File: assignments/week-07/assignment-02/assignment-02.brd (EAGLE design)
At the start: 68.6 x 53.3 mm, 6 parts

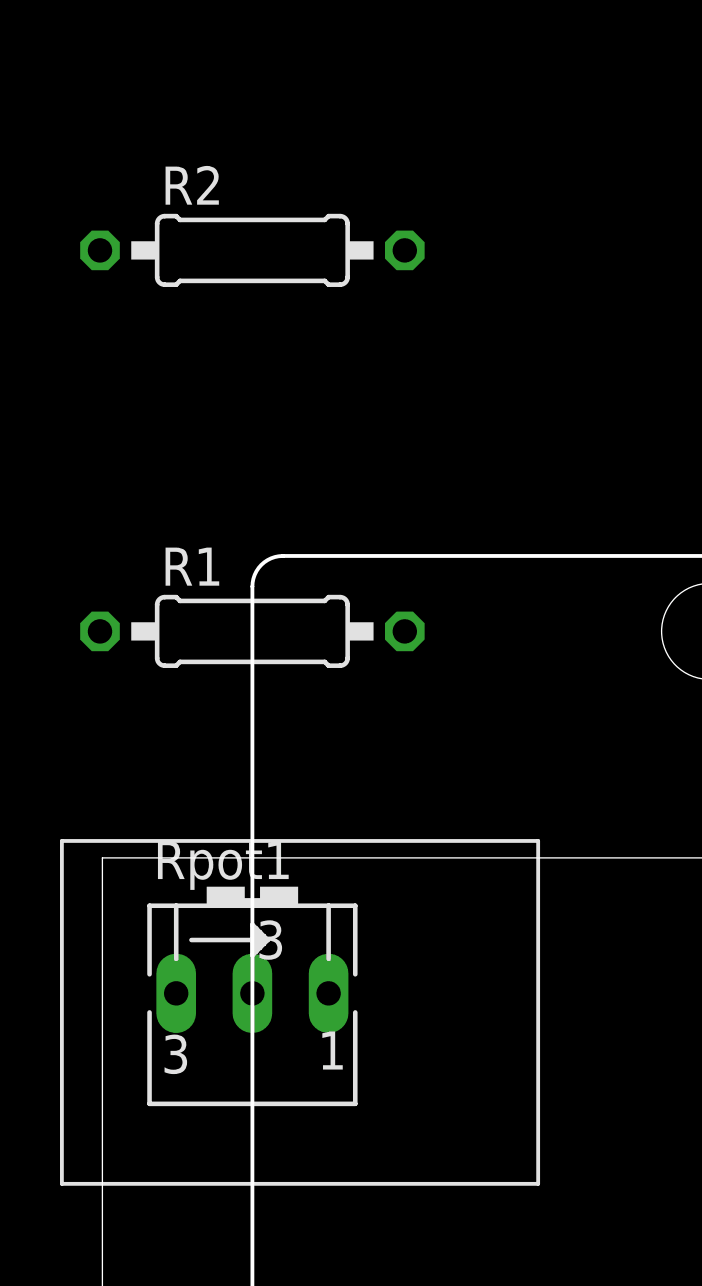
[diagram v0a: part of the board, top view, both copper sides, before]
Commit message: Remove Serial usage
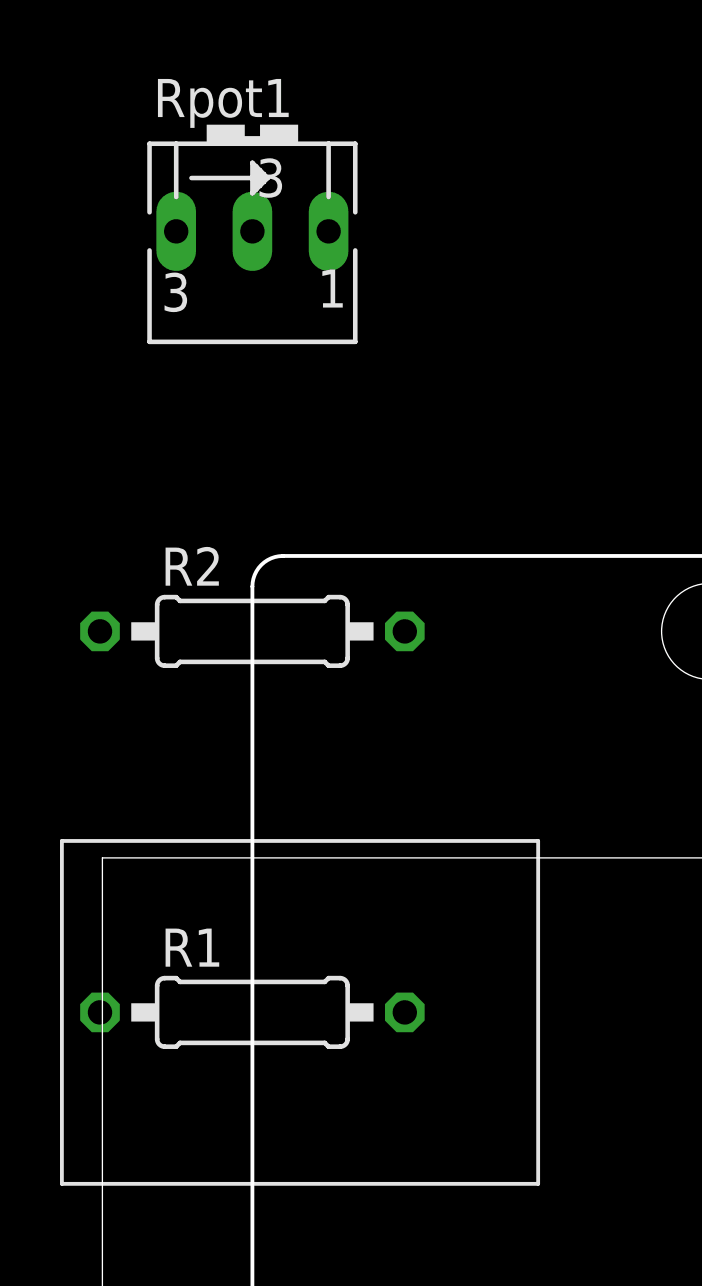
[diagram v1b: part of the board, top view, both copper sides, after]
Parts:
- moved Rpot1 25.4 mm to (5.00, 73.6)
- moved R2 12.7 mm to (5.00, 60.9)
- moved R1 12.7 mm to (5.00, 48.2)
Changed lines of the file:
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@@
 </autorouter>
 <elements>
-<element value="" name="U1" library="AUTODESK_CIRCUITS_BREADBOARD" package="ARDUINO_UNO" x="5" y="10.08"></element><element value="" name="D1" library="AUTODESK_CIRCUITS_BREADBOARD" package="LED5MM" x="5" y="22.78"></element><element value="" name="D2" library="AUTODESK_CIRCUITS_BREADBOARD" package="LED5MM" x="5" y="35.480000000000004"></element><element value="10k‎Ω" name="Rpot1" library="AUTODESK_CIRCUITS_BREADBOARD" package="B25V" x="5" y="48.18"></element><element value="220‎Ω" name="R1" library="AUTODESK_CIRCUITS_BREADBOARD" package="0207/10" x="5" y="60.879999999999995"></element><element value="220‎Ω" name="R2" library="AUTODESK_CIRCUITS_BREADBOARD" package="0207/10" x="5" y="73.58"></element></elements>
+<element value="" name="U1" library="AUTODESK_CIRCUITS_BREADBOARD" package="ARDUINO_UNO" x="5" y="10.08"></element><element value="" name="D1" library="AUTODESK_CIRCUITS_BREADBOARD" package="LED5MM" x="5" y="22.78"></element><element value="" name="D2" library="AUTODESK_CIRCUITS_BREADBOARD" package="LED5MM" x="5" y="35.480000000000004"></element><element value="220‎Ω" name="R1" library="AUTODESK_CIRCUITS_BREADBOARD" package="0207/10" x="5" y="48.18"></element><element value="220‎Ω" name="R2" library="AUTODESK_CIRCUITS_BREADBOARD" package="0207/10" x="5" y="60.879999999999995"></element><element value="10k‎Ω" name="Rpot1" library="AUTODESK_CIRCUITS_BREADBOARD" package="B25V" x="5" y="73.58"></element></elements>
 <signals>
-<signal name="N$1"><contactref element="D1" pad="A"></contactref><contactref element="U1" pad="0"></contactref><wire x1="3.73" y1="22.78" x2="68.5" y2="60.879999999999995" width="0" layer="19" extent="1-1"></wire></signal><signal name="N$2"><contactref element="Rpot1" pad="E"></contactref><contactref element="U1" pad="5V"></contactref><wire x1="2.46" y1="48.815" x2="43.1" y2="12.620000000000001" width="0" layer="19" extent="1-1"></wire></signal><signal name="N$3"><contactref element="Rpot1" pad="A"></contactref><contactref element="U1" pad="GND."></contactref><wire x1="7.54" y1="48.815" x2="48.18" y2="12.620000000000001" width="0" layer="19" extent="1-1"></wire><contactref element="R1" pad="1"></contactref><wire x1="48.18" y1="12.620000000000001" x2="-0.08000000000000007" y2="60.879999999999995" width="0" layer="19" extent="1-1"></wire><contactref element="R2" pad="1"></contactref><wire x1="-0.08000000000000007" y1="60.879999999999995" x2="-0.08000000000000007" y2="73.58" width="0" layer="19" extent="1-1"></wire></signal><signal name="N$4"><contactref element="Rpot1" pad="S"></contactref><contactref element="U1" pad="A0"></contactref><wire x1="5" y1="48.815" x2="55.8" y2="12.620000000000001" width="0" layer="19" extent="1-1"></wire></signal><signal name="N$5"><contactref element="D2" pad="A"></contactref><contactref element="U1" pad="1"></contactref><wire x1="3.73" y1="35.480000000000004" x2="65.96000000000001" y2="60.879999999999995" width="0" layer="19" extent="1-1"></wire></signal><signal name="N$6"><contactref element="D1" pad="K"></contactref><contactref element="R1" pad="2"></contactref><wire x1="6.27" y1="22.78" x2="10.08" y2="60.879999999999995" width="0" layer="19" extent="1-1"></wire></signal><signal name="N$7"><contactref element="D2" pad="K"></contactref><contactref element="R2" pad="2"></contactref><wire x1="6.27" y1="35.480000000000004" x2="10.08" y2="73.58" width="0" layer="19" extent="1-1"></wire></signal></signals>
+<signal name="N$1"><contactref element="D1" pad="A"></contactref><contactref element="U1" pad="0"></contactref><wire x1="3.73" y1="22.78" x2="68.5" y2="60.879999999999995" width="0" layer="19" extent="1-1"></wire></signal><signal name="N$2"><contactref element="U1" pad="5V"></contactref><contactref element="Rpot1" pad="E"></contactref><wire x1="43.1" y1="12.620000000000001" x2="2.46" y2="74.215" width="0" layer="19" extent="1-1"></wire></signal><signal name="N$3"><contactref element="U1" pad="GND."></contactref><contactref element="R2" pad="1"></contactref><wire x1="48.18" y1="12.620000000000001" x2="-0.08000000000000007" y2="60.879999999999995" width="0" layer="19" extent="1-1"></wire><contactref element="R1" pad="1"></contactref><wire x1="-0.08000000000000007" y1="60.879999999999995" x2="-0.08000000000000007" y2="48.18" width="0" layer="19" extent="1-1"></wire><contactref element="Rpot1" pad="A"></contactref><wire x1="-0.08000000000000007" y1="48.18" x2="7.54" y2="74.215" width="0" layer="19" extent="1-1"></wire></signal><signal name="N$4"><contactref element="U1" pad="A0"></contactref><contactref element="Rpot1" pad="S"></contactref><wire x1="55.8" y1="12.620000000000001" x2="5" y2="74.215" width="0" layer="19" extent="1-1"></wire></signal><signal name="N$5"><contactref element="D2" pad="A"></contactref><contactref element="U1" pad="1"></contactref><wire x1="3.73" y1="35.480000000000004" x2="65.96000000000001" y2="60.879999999999995" width="0" layer="19" extent="1-1"></wire></signal><signal name="N$6"><contactref element="D1" pad="K"></contactref><contactref element="R1" pad="2"></contactref><wire x1="6.27" y1="22.78" x2="10.08" y2="48.18" width="0" layer="19" extent="1-1"></wire></signal><signal name="N$7"><contactref element="D2" pad="K"></contactref><contactref element="R2" pad="2"></contactref><wire x1="6.27" y1="35.480000000000004" x2="10.08" y2="60.879999999999995" width="0" layer="19" extent="1-1"></wire></signal></signals>
 </board>
 </drawing>
